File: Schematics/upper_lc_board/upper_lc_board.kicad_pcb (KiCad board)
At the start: 4 copper layers, 69.5 x 60 mm, 120 parts, among them J1 Stack Male Edge Connector, J2 SOL_CONN, J3 PT1, J4 PT1, J5 HALL, J6 SOL_CONN, J7 Screw_Terminal_01x02, J8 USB_C_Female_USB2_Small, Q1 AO3400A, Q2 AO3400A, SW1 SW_ESP_BOOT_MODE, SW2 SW_ESP_RESET, U1 ESP32-S3-WROOM-1-N16, U2 ISO1044BDR, U3 LD1117S33TR_SOT223, U4 ID_LM66100DCKR, U5 ID_LM66100DCKR, U7 ADC_ADS131M04IPWR, U9 TVS3300DRV

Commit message: organizational work
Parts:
- added NT1: GND-TIE, NetTie:NetTie-2_SMD_Pad0.5mm, F.Cu at (185.8, 81.5)
- C20, C8: value 100uF_16V -> 100uF
- C26, C28: value 0.1uF_50V -> 0.1uF
- C27, C29: value 10uF_50V -> 10uF
- C33: value 0.1uF_10V -> 0.1uF; footprint Capacitor_SMD:C_0805_2012Metric -> Capacitor_SMD:C_0603_1608Metric
- C9: value 100uF_50V -> 100uF
- J3, J4: footprint CONNS:CONN02_530470260_MOL -> S02B_PASK_2:CONN2_S02B-PASK-2_JST
- TH1: footprint Resistor_SMD:R_0603_1608Metric_Pad0.98x0.95mm_HandSolder -> Resistor_SMD:R_0402_1005Metric
- U3: value LD1117S33TR_SOT223 -> AMS1117
- moved C16 6.05 mm to (191.1, 66.8)
- moved C24 6.05 mm to (182.6, 78.1)
- moved C28 6.05 mm to (182.8, 70.0)
- moved C31 6.05 mm to (190.2, 77.7)
- moved C29 6.05 mm to (183.4, 66.8)
- moved C34 6.05 mm to (175.8, 66.8)
- moved C15 6.05 mm to (190.2, 69.7)
- moved C25 6.05 mm to (183.4, 75.1)
- moved C26 6.05 mm to (175.2, 78.3)
- moved C27 6.05 mm to (175.8, 75.1)
- moved C30 6.05 mm to (190.4, 75.0)
- moved C32 6.05 mm to (190.2, 80.2)
- moved C33 6.05 mm to (175.2, 70.0)
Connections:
- C21 pad 1: GND -> GNDA
- C22 pad 2: GND -> GNDA
- C26 pad 1: +24V -> /Sensor Circuitry/PT-1/VIN
- C26 pad 2: GND -> GNDA
- C27 pad 1: +24V -> /Sensor Circuitry/PT-1/VIN
- C27 pad 2: GND -> GNDA
- C28 pad 1: +24V -> /Sensor Circuitry/PT-2/VIN
- C28 pad 2: GND -> GNDA
- C29 pad 1: +24V -> /Sensor Circuitry/PT-2/VIN
- C29 pad 2: GND -> GNDA
- C31 pad 1: GND -> GNDA
- C32 pad 1: GND -> GNDA
- D18 pad 1: GND -> GNDA
- D18 pad 4: GND -> GNDA
- D7 pad 1: GND -> GNDA
- D7 pad 4: GND -> GNDA
- J3 pad 1: +24V -> /Sensor Circuitry/PT-2/VIN
- J4 pad 1: +24V -> /Sensor Circuitry/PT-1/VIN
- R16 pad 1: GND -> GNDA
- R18 pad 1: GND -> GNDA
- R21 pad 1: GND -> GNDA
- R23 pad 1: GND -> GNDA
- R27 pad 2: GND -> GNDA
- TH1 pad 2: GND -> GNDA
- TP7 pad 1: SOL1_RET -> /Solenoid Driver Circuitry/TP
- TP9 pad 1: SOL2_RET -> /Solenoid Driver Circuitry/TP_1
- U7 pad 10: GND -> GNDA
- U7 pad 2: GND -> GNDA
- U7 pad 9: GND -> GNDA
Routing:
- net GND: track 203.4 -> 194.3 mm, vias 134 -> 130
- net GNDA: track 0.00 -> 9.13 mm, vias 0 -> 4
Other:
- board text added: "for V2"

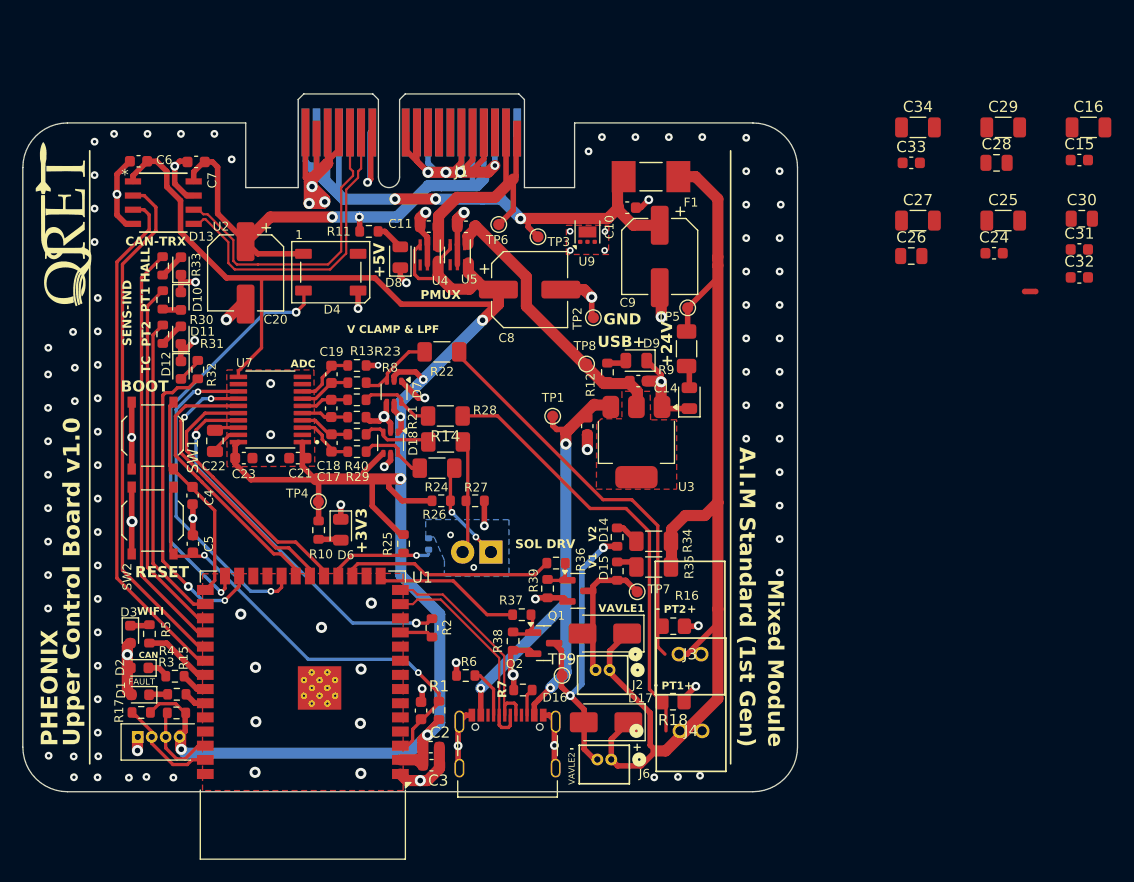
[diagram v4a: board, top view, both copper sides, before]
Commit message: move lc v2 to og folder
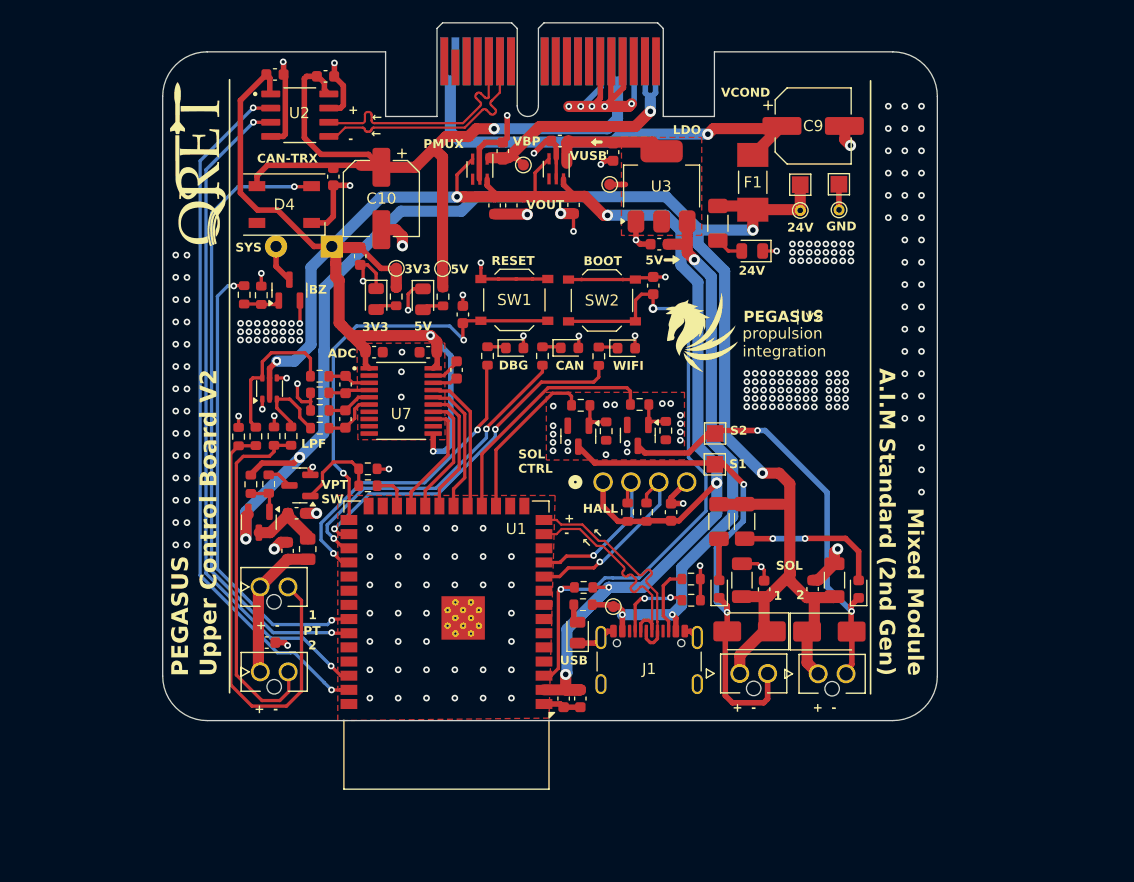
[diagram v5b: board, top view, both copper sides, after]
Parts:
- removed C28: 0.1uF, Capacitor_SMD:C_0805_2012Metric
- removed C32: 1nF, Capacitor_SMD:C_0603_1608Metric
- removed C33: 0.1uF, Capacitor_SMD:C_0603_1608Metric
- removed C34: 1uF_10V, Capacitor_SMD:C_1206_3216Metric
- removed D12: LED, LED_SMD:LED_0603_1608Metric
- removed D15: SOL1_LED (YELW), Resistor_SMD:R_0603_1608Metric
- removed D16, D17: SS34, Diode_SMD:D_SMA
- removed D18: BAV199DW, Package_TO_SOT_SMD:SOT-363_SC-70-6
- removed J8: USB_C_Female_USB2_Small, USBC-CONN:USB_C_DB-108PWB
- removed NT1: GND-TIE, NetTie:NetTie-2_SMD_Pad0.5mm
- removed R27: 1M, Resistor_SMD:R_0603_1608Metric
- removed R30, R32, R33: 150, Resistor_SMD:R_0603_1608Metric
- removed R34, R35: 4.7k, Resistor_SMD:R_1206_3216Metric_Pad1.30x1.75mm_HandSolder
- removed R36, R40: 200, Resistor_SMD:R_0603_1608Metric
- removed TH1: Thermistor, Resistor_SMD:R_0402_1005Metric
- added BZ1: Buzzer, Buzzer_Beeper:Buzzer_TDK_PS1240P02BT_D12.2mm_H6.5mm, B.Cu at (123.2, 77.5)
- added FB1: 100R, Resistor_SMD:R_0805_2012Metric, F.Cu at (121.0, 104.6)
- added G***: LOGO, LOGO, F.Cu at (156.2, 85.6)
- added G***: LOGO, LOGO, B.Cu at (120.3, 65.7)
- added Q4: 2N7002, Package_TO_SOT_SMD:SOT-23, F.Cu at (119.4, 81.4)
- added Q5: 2N7002, Package_TO_SOT_SMD:SOT-23, F.Cu at (120.3, 98.9)
- added R19: 200, Resistor_SMD:R_0603_1608Metric, F.Cu at (145.5, 91.7)
- added R20: 100k, Resistor_SMD:R_0603_1608Metric, F.Cu at (147.8, 94.0)
- added TP10: VALVE1_OUT_TP, TestPoint:TestPoint_Pad_1.5x1.5mm, F.Cu at (157.5, 97.0)
- added TP11: 24V-TP-H, TestPoint:TestPoint_THTPad_D1.0mm_Drill0.5mm, F.Cu at (165.2, 74.2)
- C10: value 0.1uF -> 100uF 16V; footprint Capacitor_SMD:C_0603_1608Metric -> Capacitor_SMD:CP_Elec_6.3x5.9
- C13: value 10uF -> 0.1uF
- C15: value 0.1uF_50V -> 1nF
- C16: value 10uF_50V -> 0.1uF; footprint Capacitor_SMD:C_1206_3216Metric -> Capacitor_SMD:C_0603_1608Metric
- C17: value 10nF -> 10uF
- C18: value 10nF -> 10uF; footprint Capacitor_SMD:C_0603_1608Metric -> Capacitor_SMD:C_1206_3216Metric
- C19: value 10nF -> 0.1uF
- C20: value 100uF -> 10uF; footprint Capacitor_SMD:CP_Elec_6.3x5.9 -> Capacitor_SMD:C_1206_3216Metric
- C21, C23: value 1uF -> 0.1uF
- C22: value 220 nF -> 0.1uF; footprint Capacitor_SMD:C_0805_2012Metric -> Capacitor_SMD:C_0603_1608Metric
- C24: value 0.1uF_50V -> 0.1uF
- C25: value 10uF_50V -> 10nF; footprint Capacitor_SMD:C_1206_3216Metric -> Capacitor_SMD:C_0603_1608Metric
- C26: value 0.1uF -> 10nF; footprint Capacitor_SMD:C_0805_2012Metric -> Capacitor_SMD:C_0603_1608Metric
- C27: value 10uF -> 0.1uF; footprint Capacitor_SMD:C_1206_3216Metric -> Capacitor_SMD:C_0603_1608Metric
- C29: value 10uF -> 1uF; footprint Capacitor_SMD:C_1206_3216Metric -> Capacitor_SMD:C_0603_1608Metric
- C30: value 0.1uF -> 220 nF; footprint Capacitor_SMD:C_0805_2012Metric -> Capacitor_SMD:C_0603_1608Metric
- C31: value 1nF -> 1uF
- C5: value 0.1uF -> 10uF
- C8: value 100uF -> 10uF; footprint Capacitor_SMD:CP_Elec_6.3x5.9 -> Capacitor_SMD:C_0603_1608Metric
- C9: value 100uF -> 100uF 35V
- D1: value FAULT_LED -> FAULT_LED (RED)
- D10: value LED -> SOL1_LED (WHT)
- D11: value LED -> BAV199DW; footprint LED_SMD:LED_0603_1608Metric -> Package_TO_SOT_SMD:SOT-363_SC-70-6
- D13: value LED -> SS34; footprint LED_SMD:LED_0603_1608Metric -> Diode_SMD:D_SMA
- D14: value SOL2_LED (YELW) -> SS34; footprint Resistor_SMD:R_0603_1608Metric -> Diode_SMD:D_SMA
- D2: value CAN_LED -> CAN_LED (WHT)
- D3: value WIFI_LED -> WIFI_LED (WHT)
- D5: value PWR_24V_LED (GRN) -> PWR_3V3_LED (GRN)
- D6: value PWR_3V3_LED (GRN) -> PWR_24V_LED (GRN)
- D7: value BAV199DW -> PWR_5V_LED (GRN); footprint Package_TO_SOT_SMD:SOT-363_SC-70-6 -> LED_SMD:LED_0805_2012Metric
- D8: value PWR_5V_LED (GRN) -> USB_LED (GRN)
- D9: value USB_LED (GRN) -> SOL2_LED (WHT); footprint LED_SMD:LED_0805_2012Metric -> LED_SMD:LED_0603_1608Metric
- J1: value Stack Male Edge Connector -> USB_C_Female_USB2_Small; footprint Connector_PCBEdge:BUS_PCIexpress_x1 -> Connector_USB:USB_C_Receptacle_GCT_USB4105-xx-A_16P_TopMnt_Horizontal
- J2: value SOL_CONN -> Stack Male Edge Connector; footprint CONNS:CONN02_530470260_MOL -> Connector_PCBEdge:BUS_PCIexpress_x1
- J3, J4: footprint S02B_PASK_2:CONN2_S02B-PASK-2_JST -> NANO-V-2-CONN:MOLEX_1053091102
- J5: value HALL -> HALL-1; footprint 53047-0460:MOLEX_53047-0460 -> NANO-H-4-CONN:CONN_SD-105313-100_04_MOL
- J6: footprint CONNS:CONN02_530470260_MOL -> NANO-V-2-CONN:MOLEX_1053091102
- J7: value Screw_Terminal_01x02 -> SOL_CONN; footprint TerminalBlock_TE-Connectivity:TerminalBlock_TE_282834-2_1x02_P2.54mm_Horizontal -> NANO-V-2-CONN:MOLEX_1053091102; moved to F.Cu
- R10: value 150 -> 200
- R11: value 510 -> 62
- R12: value 150 -> 1k
- R14: value 1k -> 62; footprint Resistor_SMD:R_1206_3216Metric_Pad1.30x1.75mm_HandSolder -> Resistor_SMD:R_0603_1608Metric
- R15: value 2.2k -> 12k; footprint Resistor_SMD:R_0603_1608Metric -> Resistor_SMD:R_1206_3216Metric_Pad1.30x1.75mm_HandSolder
- R16: value 165 -> 12k; footprint Resistor_SMD:R_0805_2012Metric_Pad1.20x1.40mm_HandSolder -> Resistor_SMD:R_1206_3216Metric_Pad1.30x1.75mm_HandSolder
- R17: value 2.2k -> 1k
- R18: value 165 -> 200; footprint Resistor_SMD:R_0805_2012Metric_Pad1.20x1.40mm_HandSolder -> Resistor_SMD:R_0603_1608Metric
- R2: value 33 -> 680
- R21: value 1.2k -> 2.2k
- R22: value 1k -> 2.2k; footprint Resistor_SMD:R_1206_3216Metric_Pad1.30x1.75mm_HandSolder -> Resistor_SMD:R_0603_1608Metric
- R23: value 1.2k -> 10k
- R24: value 1k -> 1.2k; footprint Resistor_SMD:R_1206_3216Metric_Pad1.30x1.75mm_HandSolder -> Resistor_SMD:R_0603_1608Metric
- R25: value 10k -> 1.2k
- R26: value 1M -> 200
- R28: value 1k -> 10k; footprint Resistor_SMD:R_1206_3216Metric_Pad1.30x1.75mm_HandSolder -> Resistor_SMD:R_0603_1608Metric
- R29, R37: value 200 -> 6.2k
- R3, R4: value 150 -> 270
- R31: value 150 -> 100k
- R38: value 100k -> 10k
- R39: value 100k -> 200
- R5: value 150 -> 5.1k
- R7: value 5.1k -> 3.3k
- R8: value 200 -> 12k; footprint Resistor_SMD:R_0603_1608Metric -> Resistor_SMD:R_1206_3216Metric_Pad1.30x1.75mm_HandSolder
- R9: value 4.7k -> 6.2k; footprint Resistor_SMD:R_1206_3216Metric_Pad1.30x1.75mm_HandSolder -> Resistor_SMD:R_0603_1608Metric
- TP2: value GND -> 3V3-TP
- TP3: value 24V_BP -> 24V-TP-P; footprint TestPoint:TestPoint_Pad_D1.0mm -> TestPoint:TestPoint_Pad_1.5x1.5mm
- TP4: value 3V3 -> 5V-TP
- TP5: value 24V -> GND-TP-P; footprint TestPoint:TestPoint_Pad_D1.0mm -> TestPoint:TestPoint_Pad_1.5x1.5mm
- TP7: value VALVE1_OUT_TP -> GND-TP-H; footprint TestPoint:TestPoint_Pad_D1.0mm -> TestPoint:TestPoint_THTPad_D1.0mm_Drill0.5mm
- TP8: value 3V3_USB -> VALVE2_OUT_TP; footprint TestPoint:TestPoint_Pad_D1.0mm -> TestPoint:TestPoint_Pad_1.5x1.5mm
- TP9: value VALVE2_OUT_TP -> 3V3_USB
- U2: footprint ul_ISO1044BDR:SOIC_1044BDR_TEX -> ul_ISO1044BDR:SOIC127P600X175-8N
- U3: value AMS1117 -> AMS1117-3.3
- U9: value TVS3300DRV -> DMP4065S-7; footprint Package_SON:WSON-6-1EP_2x2mm_P0.65mm_EP1x1.6mm -> Package_TO_SOT_SMD:SOT-23
- moved C24 68.8 mm to (119.2, 104.8), turned to 90 degrees
- moved C31 63.9 mm to (127.0, 86.9), turned to 180 degrees
- moved C25 60.8 mm to (124.4, 89.8), turned to 90 degrees
- moved D13 60.6 mm to (160.6, 112.0), turned to 180 degrees
- moved C20 59.6 mm to (168.3, 107.4), turned to 90 degrees
- moved C30 57.7 mm to (134.4, 88.5), turned to 90 degrees
- moved C29 55.4 mm to (131.8, 87.0)
- moved D10 54.8 mm to (157.9, 108.2), turned to 90 degrees
- moved J2 54.8 mm to (152.2, 60.9), turned to 180 degrees
- moved R15 53.8 mm to (160.2, 102.1), turned to 90 degrees
- moved C26 52.8 mm to (124.4, 92.9), turned to -90 degrees
- moved C15 52.6 mm to (137.8, 73.8), turned to -90 degrees
- moved C27 52.6 mm to (123.3, 71.2), turned to 90 degrees
- moved C5 51.5 mm to (148.4, 69.0)
- moved D3 51.4 mm to (149.6, 86.6), turned to 0 degrees
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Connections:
- net /ESP Breakout Cirucitry/ESP32_IO0 renamed /ESP32-S3 Breakout Circuitry/ESP32_IO0
- net ADC_MISO renamed SPI_MISO
- C1 pad 1: /ESP Breakout Cirucitry/ESP32_EN -> /ESP32-S3 Breakout Circuitry/ESP32_EN
- C10 pad 1: +24V_BP -> +5V
- C13 pad 1: 5V_USB -> VPT
- C14 pad 1: /Power Circuitry/3V3_USB -> 5V_USB
- C15 pad 1: +24V -> +3V3
- C16 pad 1: +24V -> +3V3
- C17 pad 1: /Sensor Circuitry/TC_N_CLAMPED -> +3V3
- C17 pad 2: /Sensor Circuitry/TC_P_CLAMPED -> GND
- C18 pad 1: Net-(U7-AIN1N) -> +24V
- C18 pad 2: /Sensor Circuitry/PT1_CLAMPED -> GND
- C19 pad 1: Net-(U7-AIN2N) -> +24V
- C19 pad 2: /Sensor Circuitry/PT2_CLAMPED -> GND
- C20 pad 1: +5V -> +24V
- C21 pad 1: GNDA -> +24V
- C21 pad 2: +3V3 -> GND
- C22 pad 1: Net-(U7-CAP) -> +3V3
- C22 pad 2: GNDA -> GND
- C23 pad 1: GND -> +3V3
- C23 pad 2: +3V3 -> GND
- C24 pad 1: +24V -> VPT
- C25 pad 1: +24V -> Net-(U7-AIN0N)
- C25 pad 2: GND -> /Sensing Circuitry/PT1_CLAMPED
- C26 pad 1: /Sensor Circuitry/PT-1/VIN -> Net-(U7-AIN1N)
- C26 pad 2: GNDA -> /Sensing Circuitry/PT2_CLAMPED
- C27 pad 1: /Sensor Circuitry/PT-1/VIN -> GND
- C27 pad 2: GNDA -> +5V
- C29 pad 1: /Sensor Circuitry/PT-2/VIN -> GND
- C29 pad 2: GNDA -> +3V3
- C30 pad 1: /Sensor Circuitry/TC_N -> Net-(U7-CAP)
- C30 pad 2: /Sensor Circuitry/TC_P -> GND
- C31 pad 1: GNDA -> GND
- C31 pad 2: /Sensor Circuitry/TC_P -> +3V3
- C5 pad 1: GND -> /Power Circuitry/3V3_USB
- C5 pad 2: /ESP Breakout Cirucitry/ESP32_EN -> GND
- C8 pad 1: +3V3 -> Net-(U9-D)
- C9 pad 1: Net-(C9-Pad1) -> +24V_BP
- D10 pad 1: GND -> SOL1_RET
- D11 pad 2: Net-(D11-A) -> +3V3
- D13 pad 1: GND -> +24V
- D13 pad 2: Net-(D13-A) -> SOL1_RET
- D14 pad 1: SOL2_RET -> +24V
- D14 pad 2: Net-(D14-A) -> SOL2_RET
- D4 pad 2: /ESP Breakout Cirucitry/GPIO_45 -> unconnected-(D4-DOUT-Pad2)
- D4 pad 4: unconnected-(D4-DIN-Pad4) -> /ESP32-S3 Breakout Circuitry/GPIO_42
- D7 pad 1: GNDA -> GND
- D7 pad 2: +3V3 -> Net-(D7-A)
- D9 pad 1: GND -> SOL2_RET
- F1 pad 2: Net-(C9-Pad1) -> +24V_BP
- J1 pad A1: /Power Circuitry/3V3_BP -> GND
- J1 pad A4: +5V -> 5V_USB
- J1 pad A5: +5V -> Net-(J1-CC1)
- J1 pad A6: GND -> /ESP32-S3 Breakout Circuitry/USB_P
- J1 pad A7: unconnected-(J1-3.3V_B-PadA7)_0 -> /ESP32-S3 Breakout Circuitry/USB_N
- J1 pad A9: GND -> 5V_USB
- J1 pad B1: unconnected-(J1-BATT_A-PadB1)_1 -> GND
- J1 pad B4: GND -> 5V_USB
- J1 pad B5: GND -> Net-(J1-CC2)
- J1 pad B6: GND -> /ESP32-S3 Breakout Circuitry/USB_P
- J1 pad B7: unconnected-(J1-BATT_B-PadB7) -> /ESP32-S3 Breakout Circuitry/USB_N
- J1 pad B9: unconnected-(J1-BATT_B-PadB7)_1 -> 5V_USB
- J3 pad 1: /Sensor Circuitry/PT-2/VIN -> VPT
- J3 pad 2: /Sensor Circuitry/PT2 -> Net-(J3-Pin_2)
- J4 pad 1: /Sensor Circuitry/PT-1/VIN -> VPT
- J4 pad 2: /Sensor Circuitry/PT1 -> Net-(J4-Pin_2)
- J5 pad 1: GND -> +3V3
- J5 pad 2: HALL_SCL -> HALL_SDA
- J5 pad 3: HALL_SDA -> HALL_SCL
- J5 pad 4: +3V3 -> GND
- J7 pad 1: /Sensor Circuitry/TC_P -> +24V
- J7 pad 2: /Sensor Circuitry/TC_N -> SOL1_RET
- R1 pad 2: /ESP Breakout Cirucitry/ESP32_EN -> /ESP32-S3 Breakout Circuitry/ESP32_EN
- R10 pad 1: Net-(D6-A) -> Net-(Q4-G)
- R10 pad 2: +3V3 -> BUZZ_IN
- R11 pad 1: Net-(D8-A) -> GND
- R11 pad 2: +5V -> Net-(J4-Pin_2)
- R12 pad 1: /Power Circuitry/3V3_USB -> Net-(J4-Pin_2)
- R12 pad 2: Net-(D9-A) -> Net-(D11A-K3A4)
- R13 pad 1: /Sensor Circuitry/PT1_CLAMPED -> /Sensing Circuitry/PT1_CLAMPED
- R13 pad 2: Net-(D7A-K3A4) -> Net-(D11A-K3A4)
- R14 pad 1: /Sensor Circuitry/PT1 -> GND
- R14 pad 2: Net-(D7A-K3A4) -> Net-(J3-Pin_2)
- R15 pad 1: HALL_SDA -> Net-(D9-A)
- R15 pad 2: +3V3 -> +24V
- R16 pad 1: GNDA -> Net-(D10-A)
- R16 pad 2: /Sensor Circuitry/PT2 -> +24V
- R17 pad 1: +3V3 -> Net-(J3-Pin_2)
- R17 pad 2: HALL_SCL -> Net-(D11B-K1A2)
- R18 pad 1: GNDA -> /Sensing Circuitry/PT2_CLAMPED
- R18 pad 2: /Sensor Circuitry/PT1 -> Net-(D11B-K1A2)
- R2 pad 1: /ESP Breakout Cirucitry/GPIO_18 -> /ESP32-S3 Breakout Circuitry/GPIO_37
- R2 pad 2: ADC_CLKIN -> Net-(D1-K)
- R21 pad 1: GNDA -> HALL_SDA
- R21 pad 2: Net-(U7-AIN1N) -> +3V3
- R22 pad 1: /Sensor Circuitry/PT2 -> +3V3
- R22 pad 2: Net-(D7B-K1A2) -> HALL_SCL
- R23 pad 1: GNDA -> Net-(Q5-D)
- R23 pad 2: Net-(U7-AIN2N) -> Net-(U9-G)
- R24 pad 1: Net-(D18A-K3A4) -> GND
- R24 pad 2: /Sensor Circuitry/TC_P -> Net-(U7-AIN0N)
- R25 pad 1: TEMP_SENSE -> GND
- R25 pad 2: +3V3 -> Net-(U7-AIN1N)
- R26 pad 1: +3V3 -> Net-(Q2-G)
- R26 pad 2: /Sensor Circuitry/TC_P -> VALVE2_CTRL
- R28 pad 1: Net-(D18B-K1A2) -> GND
- R28 pad 2: /Sensor Circuitry/TC_N -> Net-(Q4-G)
- R29 pad 1: Net-(D18A-K3A4) -> 5V_USB
- R29 pad 2: /Sensor Circuitry/TC_P_CLAMPED -> Net-(D8-A)
- R3 pad 1: /ESP Breakout Cirucitry/GPIO_42 -> /ESP32-S3 Breakout Circuitry/GPIO_36
- R3 pad 2: Net-(D1-K) -> Net-(D2-K)
- R31 pad 1: PT2_LED -> GND
- R31 pad 2: Net-(D11-A) -> Net-(Q2-G)
- R37 pad 1: Net-(Q2-G) -> Net-(U9-G)
- R37 pad 2: VALVE2_CTRL -> +24V
- R38 pad 2: Net-(Q2-G) -> Net-(Q5-G)
- R39 pad 1: GND -> VPT-SW
- R39 pad 2: Net-(Q1-G) -> Net-(Q5-G)
- R4 pad 1: /ESP Breakout Cirucitry/GPIO_41 -> /ESP32-S3 Breakout Circuitry/GPIO_35
- R4 pad 2: Net-(D2-K) -> Net-(D3-K)
- R5 pad 1: /ESP Breakout Cirucitry/GPIO_40 -> Net-(J1-CC1)
- R5 pad 2: Net-(D3-K) -> GND
- R6 pad 1: Net-(J8-CC1) -> Net-(J1-CC2)
- R7 pad 1: Net-(J8-CC2) -> Net-(D5-A)
- R7 pad 2: GND -> +3V3
- R8 pad 1: /Sensor Circuitry/PT2_CLAMPED -> Net-(D6-A)
- R8 pad 2: Net-(D7B-K1A2) -> +24V
- R9 pad 1: Net-(D5-A) -> Net-(D7-A)
- R9 pad 2: +24V -> +5V
- SW2 pad 2: /ESP Breakout Cirucitry/ESP32_EN -> /ESP32-S3 Breakout Circuitry/ESP32_EN
- TP2 pad 1: GND -> +3V3
- TP3 pad 1: +24V_BP -> +24V
- TP4 pad 1: +3V3 -> +5V
- TP5 pad 1: +24V -> GND
- TP7 pad 1: /Solenoid Driver Circuitry/TP -> GND
- TP8 pad 1: /Power Circuitry/3V3_USB -> SOL2_RET
- TP9 pad 1: /Solenoid Driver Circuitry/TP_1 -> /Power Circuitry/3V3_USB
- U1 pad 10: unconnected-(U1-IO17-Pad10) -> HALL_SCL
- U1 pad 11: /ESP Breakout Cirucitry/GPIO_18 -> HALL_SDA
- U1 pad 13: /ESP Breakout Cirucitry/USB_N -> /ESP32-S3 Breakout Circuitry/USB_N
- U1 pad 14: /ESP Breakout Cirucitry/USB_P -> /ESP32-S3 Breakout Circuitry/USB_P
- U1 pad 15: VALVE2_CTRL -> /ESP32-S3 Breakout Circuitry/GPIO_03
- U1 pad 16: unconnected-(U1-IO46-Pad16) -> /ESP32-S3 Breakout Circuitry/GPIO_46
- U1 pad 18: TEMP_SENSE -> VALVE2_CTRL
- U1 pad 19: ADC_MOSI -> ADC_CLKIN
- U1 pad 20: ADC_SCLK -> SPI_MOSI
- U1 pad 22: ADC_DREADY -> SPI_SCLK
- U1 pad 23: unconnected-(U1-IO21-Pad23) -> ADC_DRDY
- U1 pad 24: unconnected-(U1-IO47-Pad24) -> VPT-SW
- U1 pad 25: TC_LED -> unconnected-(U1-IO48-Pad25)
- U1 pad 26: /ESP Breakout Cirucitry/GPIO_45 -> /ESP32-S3 Breakout Circuitry/GPIO_45
- U1 pad 28: PT2_LED -> /ESP32-S3 Breakout Circuitry/GPIO_35
- U1 pad 29: PT1_LED -> /ESP32-S3 Breakout Circuitry/GPIO_36
- U1 pad 3: /ESP Breakout Cirucitry/ESP32_EN -> /ESP32-S3 Breakout Circuitry/ESP32_EN
- U1 pad 30: HALL_LED -> /ESP32-S3 Breakout Circuitry/GPIO_37
- U1 pad 31: /ESP Breakout Cirucitry/GPIO_38 -> /ESP32-S3 Breakout Circuitry/GPIO_38
- U1 pad 32: /ESP Breakout Cirucitry/GPIO_39 -> /ESP32-S3 Breakout Circuitry/GPIO_39
- U1 pad 33: /ESP Breakout Cirucitry/GPIO_40 -> /ESP32-S3 Breakout Circuitry/GPIO_40
- U1 pad 34: /ESP Breakout Cirucitry/GPIO_41 -> BUZZ_IN
- U1 pad 35: /ESP Breakout Cirucitry/GPIO_42 -> /ESP32-S3 Breakout Circuitry/GPIO_42
- U1 pad 38: HALL_SDA -> /ESP32-S3 Breakout Circuitry/GPIO_02
- U1 pad 39: HALL_SCL -> /ESP32-S3 Breakout Circuitry/GPIO_01
- U2 pad 2: /ESP Breakout Cirucitry/GPIO_38 -> /ESP32-S3 Breakout Circuitry/GPIO_01
- U2 pad 3: /ESP Breakout Cirucitry/GPIO_39 -> /ESP32-S3 Breakout Circuitry/GPIO_02
- U2 pad 5: CAN_- -> CAN_N
- U2 pad 6: CAN_+ -> CAN_P
- U7 pad 10: GNDA -> GND
- U7 pad 13: ADC_DREADY -> ADC_DRDY
- U7 pad 14: ADC_SCLK -> SPI_SCLK
- U7 pad 16: ADC_MOSI -> SPI_MOSI
- U7 pad 2: GNDA -> GND
- U7 pad 3: /Sensor Circuitry/TC_P_CLAMPED -> /Sensing Circuitry/PT1_CLAMPED
- U7 pad 4: /Sensor Circuitry/TC_N_CLAMPED -> Net-(U7-AIN0N)
- U7 pad 6: /Sensor Circuitry/PT1_CLAMPED -> /Sensing Circuitry/PT2_CLAMPED
- U7 pad 7: /Sensor Circuitry/PT2_CLAMPED -> GND
- U7 pad 8: Net-(U7-AIN2N) -> GND
- U7 pad 9: GNDA -> GND
- U9 pad 1: GND -> Net-(U9-G)
- U9 pad 2: GND -> +24V
- U9 pad 3: GND -> Net-(U9-D)
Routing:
- net /ESP32-S3 Breakout Circuitry/GPIO_01: track 0.00 -> 63.1 mm, vias 0 -> 2
- net /ESP32-S3 Breakout Circuitry/GPIO_02: track 0.00 -> 60.4 mm, vias 0 -> 2
- net /ESP32-S3 Breakout Circuitry/ESP32_EN: track 0.00 -> 58.5 mm, vias 0 -> 2
- net /ESP32-S3 Breakout Circuitry/GPIO_42: track 0.00 -> 56.7 mm, vias 0 -> 2
- net +24V: track 100.3 -> 154.2 mm, vias 0 -> 4
- net GND: track 194.3 -> 146.4 mm, vias 130 -> 275
- net /ESP Breakout Cirucitry/GPIO_38: track 46.6 -> 0.00 mm
- net /ESP Breakout Cirucitry/GPIO_39: track 46.4 -> 0.00 mm
- net /ESP Breakout Cirucitry/ESP32_EN: track 41.8 -> 0.00 mm, vias 2 -> 0
- net BUZZ_IN: track 0.00 -> 41.3 mm, vias 0 -> 2
- net Net-(J4-Pin_2): track 0.00 -> 40.8 mm
- net /Sensor Circuitry/PT1: track 39.8 -> 0.00 mm
- net HALL_LED: track 37.2 -> 0.00 mm
- net /ESP Breakout Cirucitry/GPIO_45: track 37.2 -> 0.00 mm, vias 2 -> 0
- net /Sensor Circuitry/PT2: track 36.3 -> 0.00 mm
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- removed copper zone on B.Cu, net GND
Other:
- outline, holes or cut-outs redrawn
- board text added: "+ -"
- board text added: "- SC SD +"
- board text added: "1"
- board text added: "2"
- board text added: "24V"
- board text added: "5V"
- board text added: "A.I.M Standard (2nd Gen)"
- board text added: "BZ"
- board text added: "DBG"
- board text added: "LDO"
- board text added: "LPF"
- board text added: "PEGASUS"
- board text added: "PT"
- board text added: "PT-1"
- board text added: "PT-2"
- board text added: "Pegasus QRET March 2026 Jeevan Sanchez"
- board text added: "S1"
- board text added: "S2"
- board text added: "SOL"
- board text added: "SOL CTRL"
- board text added: "SOL-1"
- board text added: "SOL-2"
- board text added: "SYS"
- board text added: "USB"
- board text added: "Upper Control Board V2"
- board text added: "VBP"
- board text added: "VCOND"
- board text added: "VOUT"
- board text added: "VPT SW"
- board text added: "VUSB"
- board text added: "bzz"
- board text added: "https://github.com/ Queens-Rocket-Engineering-Team /av-prop-integration"
- board text added: "propulsion integration"
- board text added: "| v2"
- board text added: "←"
- board text removed: "+"
- board text removed: "+24V"
- board text removed: "+3V3"
- board text removed: "+5V"
- board text removed: "-"
- board text removed: "A.I.M Standard (1st Gen)"
- board text removed: "FAULT"
- board text removed: "J2-HALL"
- board text removed: "PCB Edge"
- board text removed: "PHEONIX"
- board text removed: "PT1"
- board text removed: "PT2"
- board text removed: "Pheonix V1.0 QRET Dec 2025 Jeevan Sanchez Tristan Alderson"
- board text removed: "SCL"
- board text removed: "SDA"
- board text removed: "SENS-IND"
- board text removed: "SOL DRV"
- board text removed: "TC"
- board text removed: "U7"
- board text removed: "USB+"
- board text removed: "Upper Control Board v1.0"
- board text removed: "V CLAMP & LPF"
- board text removed: "V1"
- board text removed: "V2"
- board text removed: "VAVLE1"
- board text removed: "VAVLE2"
- board text removed: "for V2"

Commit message: final upper control board
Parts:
- removed C18, C20: 10uF, Capacitor_SMD:C_1206_3216Metric
- BZ1: value Buzzer -> PS1240P02BT; footprint Buzzer_Beeper:Buzzer_TDK_PS1240P02BT_D12.2mm_H6.5mm -> footprints:Buzzer_12.6x9.5RM5.0
- J3, J4: value PT1 -> PT; moved to B.Cu
- J6, J7: moved to B.Cu
- R15, R16: footprint Resistor_SMD:R_1206_3216Metric_Pad1.30x1.75mm_HandSolder -> Resistor_SMD:R_0603_1608Metric
- moved R1 28.2 mm to (153.7, 81.0), turned to -90 degrees
- moved TP8 16.2 mm to (169.8, 104.9)
- moved R15 8.67 mm to (167.3, 107.1), turned to 180 degrees
- moved TP10 8.09 mm to (158.8, 105.0)
- moved R16 6.10 mm to (161.3, 107.2), turned to 0 degrees
- moved C24 4.95 mm to (122.6, 101.2)
- moved J4 4.92 mm to (120.7, 105.1), turned to 180 degrees
- moved J3 4.24 mm to (120.7, 114.1), turned to 180 degrees
- moved FB1 4.11 mm to (120.1, 100.6), turned to 0 degrees
- moved C13 2.60 mm to (119.8, 112.2), turned to 180 degrees
- moved TP9 2.42 mm to (145.9, 70.9)
- moved J6 2.40 mm to (168.5, 114.1), turned to 180 degrees
- moved J7 1.69 mm to (160.0, 114.1), turned to 180 degrees
- moved BZ1 1.38 mm to (124.5, 77.9)
- moved C21 1.12 mm to (167.3, 108.7), turned to 0 degrees
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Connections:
- R11 pad 2: Net-(J4-Pin_2) -> Net-(J3-Pin_2)
- R12 pad 1: Net-(J4-Pin_2) -> Net-(J3-Pin_2)
- R14 pad 2: Net-(J3-Pin_2) -> Net-(J4-Pin_2)
- R17 pad 1: Net-(J3-Pin_2) -> Net-(J4-Pin_2)
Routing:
- net Net-(J4-Pin_2): track 40.8 -> 15.5 mm
- net +24V: track 154.2 -> 137.9 mm
- net +3V3: track 206.1 -> 191.1 mm, vias 8 -> 7
- net SOL1_RET: track 44.9 -> 30.3 mm, vias 2 -> 0
- net Net-(D9-A): track 13.3 -> 1.55 mm, vias 2 -> 0
- net Net-(J3-Pin_2): track 32.6 -> 23.0 mm
- net /ESP32-S3 Breakout Circuitry/ESP32_EN: track 58.5 -> 50.7 mm
- net /ESP32-S3 Breakout Circuitry/GPIO_02: track 60.4 -> 63.4 mm
- net SOL2_RET: track 38.6 -> 41.3 mm, vias 2 -> 0
- net /ESP32-S3 Breakout Circuitry/GPIO_01: track 63.1 -> 65.8 mm
- net +24V_BP: track 39.8 -> 37.4 mm
- net Net-(D10-A): track 3.70 -> 1.29 mm
- net GND: track 146.4 -> 144.0 mm, vias 275 -> 258
- net Net-(U9-D): track 6.42 -> 4.27 mm
- net VPT: track 12.9 -> 14.9 mm
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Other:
- board text added: "- +"
- board text removed: "S1"
- board text removed: "S2"
- board text removed: "SYS"
- board text removed: "https://github.com/ Queens-Rocket-Engineering-Team /av-prop-integration"

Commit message: actual final updates
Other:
- board text added: "Pegasus QRET March 2026 Jeevan Sanchez Tristan Alderson"
- board text removed: "Pegasus QRET March 2026 Jeevan Sanchez"
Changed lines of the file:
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@@
 	(paper "A4")
 	(title_block
-		(title "Pegasus")
+		(title "QRET 25-26 SRAD Hybrid Upper Control Module")
+		(rev "V0.2.0")
 		(company "Queen's Rocket Engineering Team")
-		(comment 1 "Upper Control Board V2")
-		(comment 2 "Jeevan Sanchez")
+		(comment 1 "Contributors: Jeevan Sanchez, Tristan Alderson")
 	)
 	(layers
@@
 		)
 	)
-	(gr_text "Pegasus\nQRET March 2026\n\nJeevan Sanchez\n"
+	(gr_text "Pegasus\nQRET March 2026\n\nJeevan Sanchez\nTristan Alderson\n"
 		(at 142 72.195 0)
 		(layer "B.SilkS")

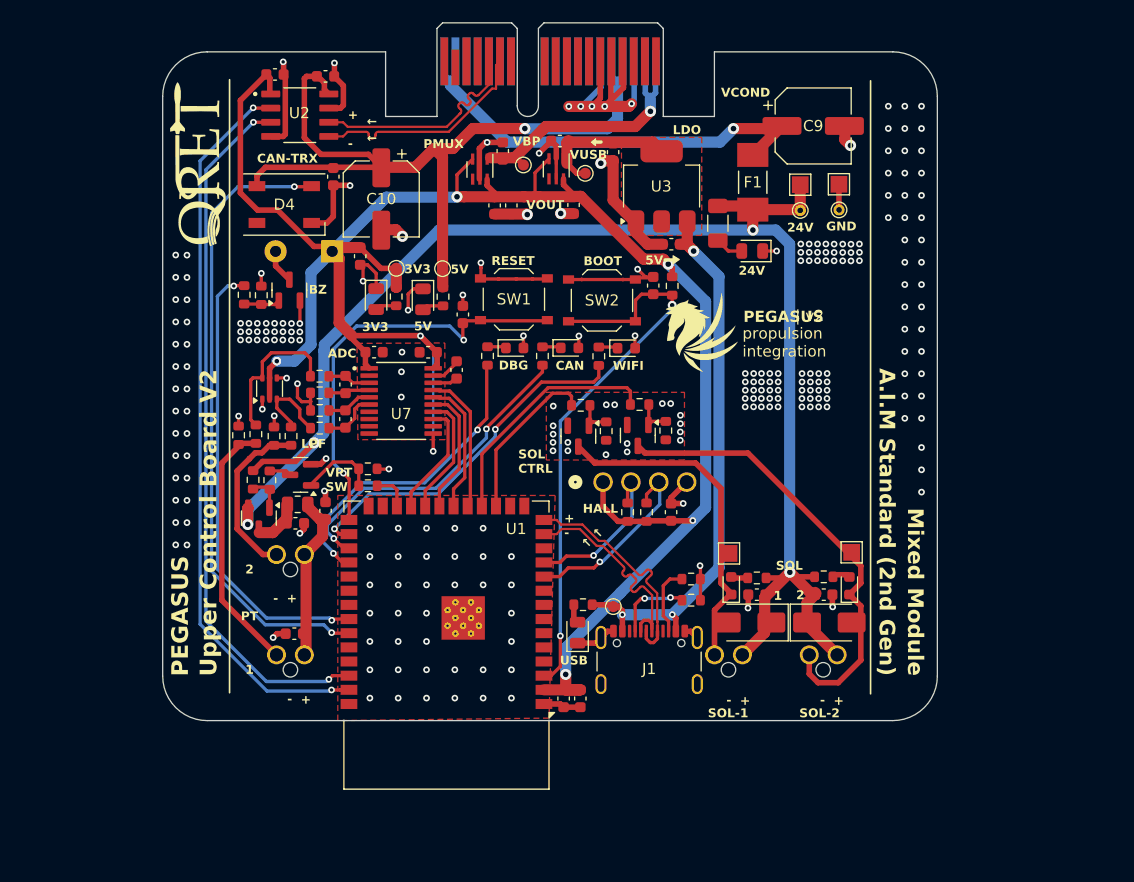
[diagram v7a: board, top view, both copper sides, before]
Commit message: final upper control board in cart, fixed HALL connector
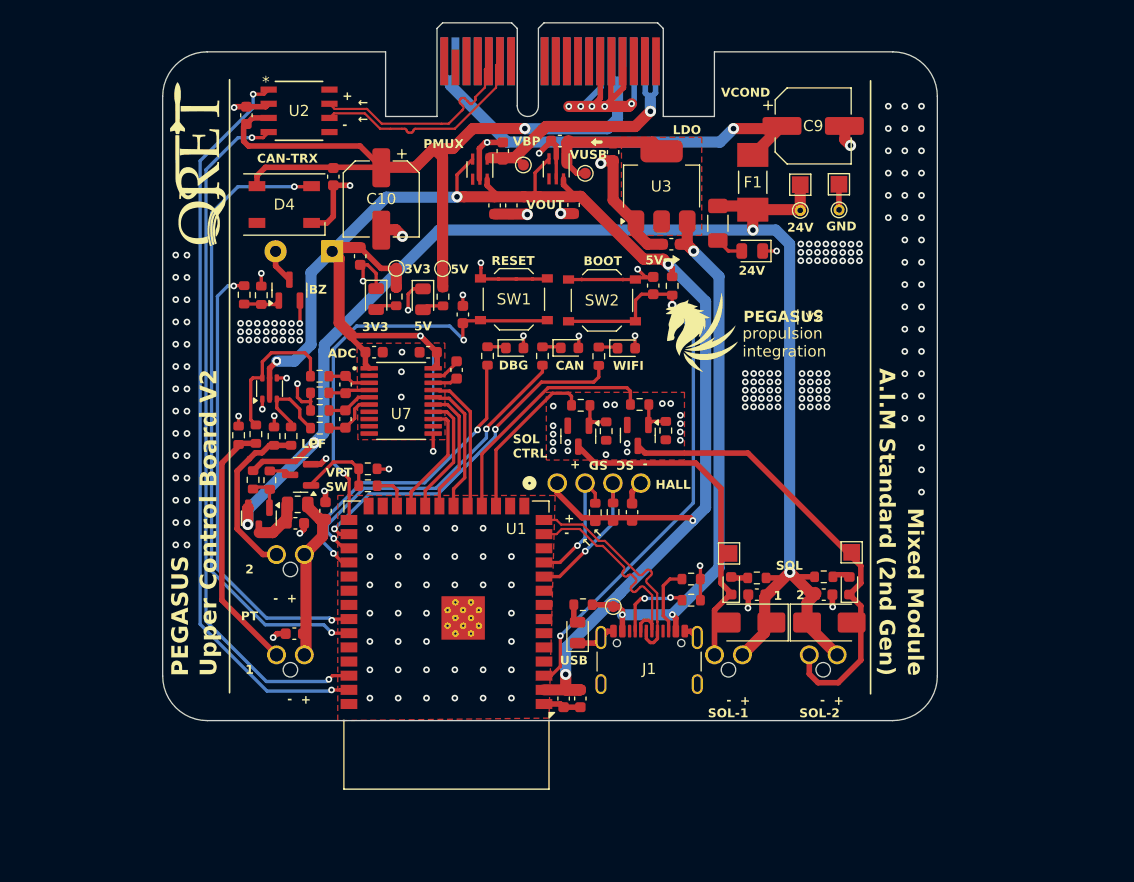
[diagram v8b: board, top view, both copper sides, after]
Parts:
- removed C7: 0.1uF, Capacitor_SMD:C_0603_1608Metric
- C6: value 0.1uF -> 100nF
- U2: value ISO1044BDR -> TCAN1051HGVDR; footprint ul_ISO1044BDR:SOIC127P600X175-8N -> ul_ISO1044BDR:SOIC_1044BDR_TEX
- moved C6 4.48 mm to (115.5, 65.7), turned to -90 degrees
- moved J5 4.12 mm to (143.4, 98.7)
- moved C22 3.50 mm to (150.1, 101.3)
- moved R22 3.00 mm to (148.4, 101.3)
- moved R21 2.90 mm to (146.8, 101.3)
- moved U2 0.40 mm to (120.2, 65.3)
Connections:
- C6 pad 1: +3V3 -> GND
- C6 pad 2: GND -> +5V
- U2 pad 1: +3V3 -> /ESP32-S3 Breakout Circuitry/GPIO_01
- U2 pad 2: /ESP32-S3 Breakout Circuitry/GPIO_01 -> GND
- U2 pad 3: /ESP32-S3 Breakout Circuitry/GPIO_02 -> +5V
- U2 pad 4: GND -> /ESP32-S3 Breakout Circuitry/GPIO_02
- U2 pad 5: CAN_N -> unconnected-(U2-NC-Pad5)
- U2 pad 6: CAN_P -> CAN_N
- U2 pad 7: GND -> CAN_P
- U2 pad 8: +5V -> unconnected-(U2-S-Pad8)
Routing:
- net +3V3: track 191.1 -> 170.7 mm
- net GND: track 144.0 -> 132.5 mm, vias 258 -> 256
- net HALL_SCL: track 16.8 -> 13.6 mm
- net HALL_SDA: track 13.6 -> 11.7 mm
- net /ESP32-S3 Breakout Circuitry/ESP32_EN: track 50.7 -> 52.3 mm
- net /ESP32-S3 Breakout Circuitry/GPIO_01: track 65.8 -> 67.0 mm
- net /ESP32-S3 Breakout Circuitry/GPIO_02: track 63.4 -> 62.8 mm
